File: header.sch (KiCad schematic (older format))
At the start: 19 parts, among them J1 Conn_01x10, J2 Conn_01x08, J3 Conn_01x06, J4 Conn_01x08, SW6 SW_Push, U1 ICE40HX4K-TQ144, U8 TXS0108EPW, U9 TXS0108EPW

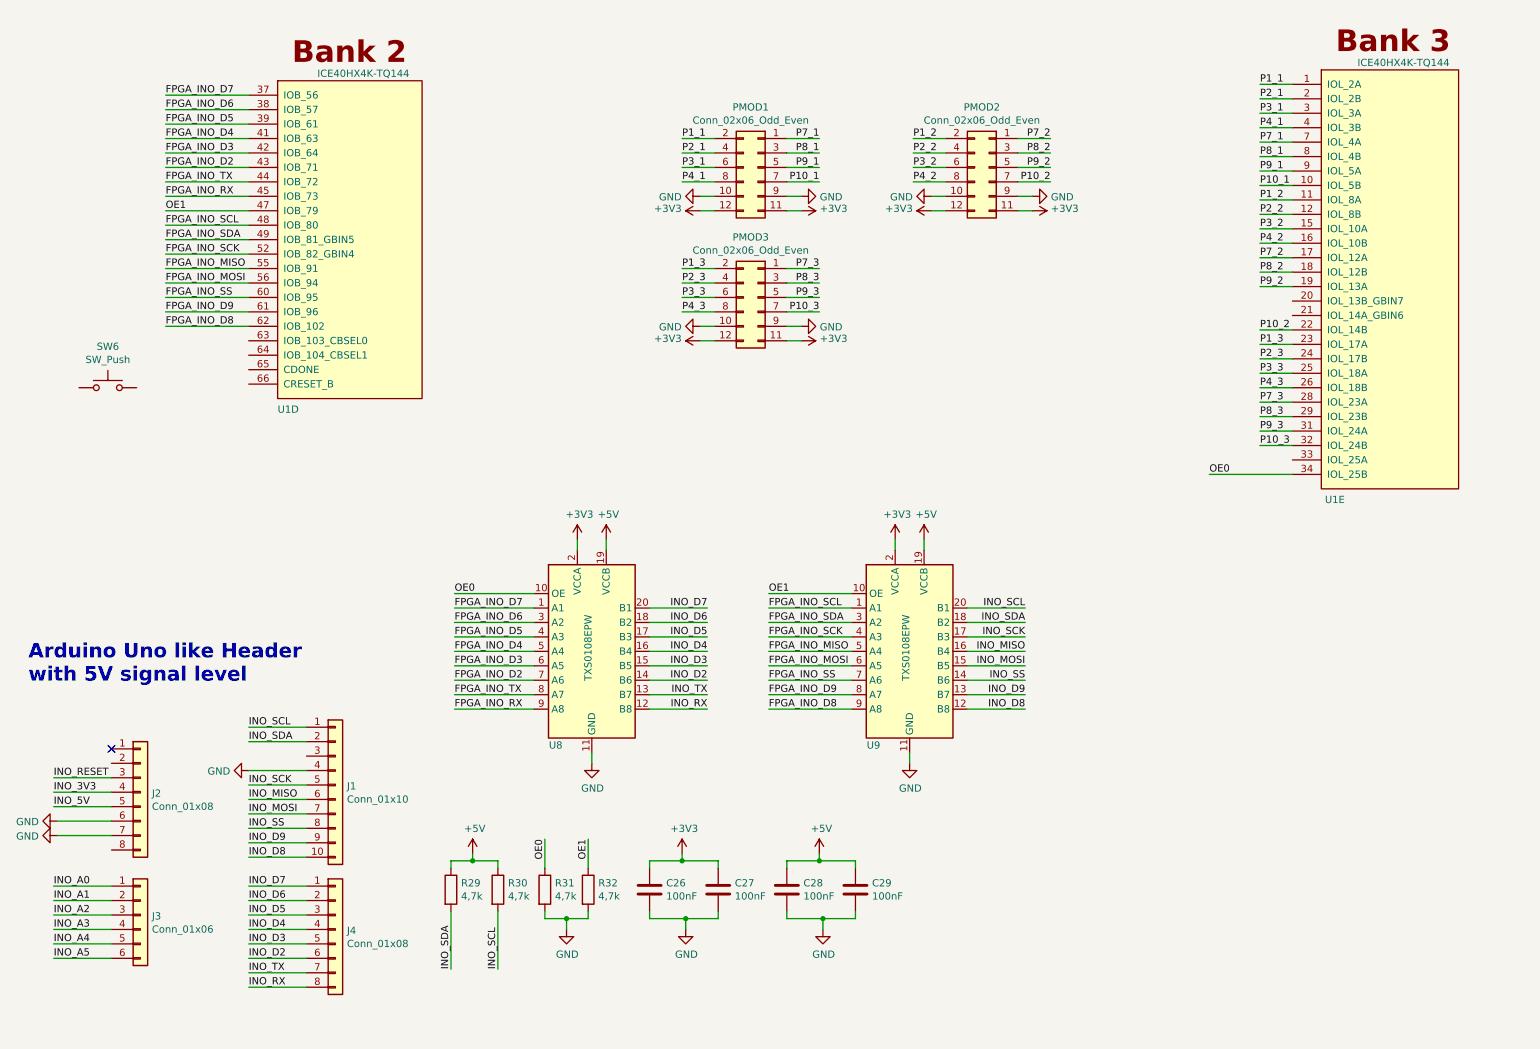
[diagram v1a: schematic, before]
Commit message: Continued on Programmer, moved the header signals around the package to free some space for a fully featured UART/RS232(TTL)
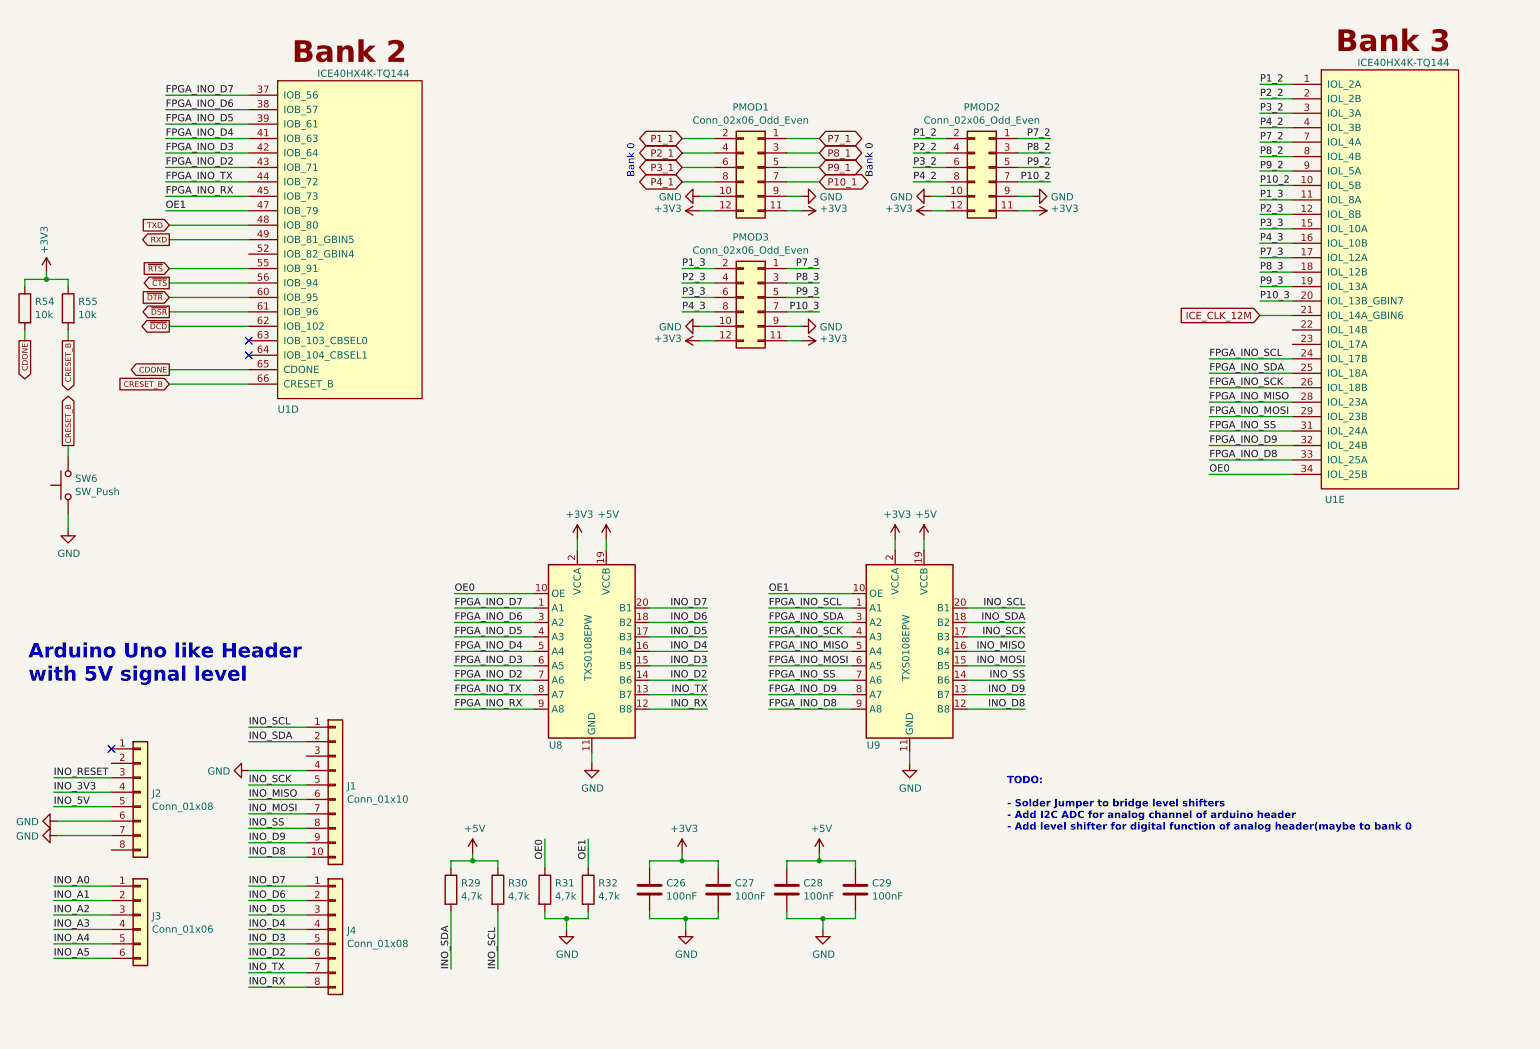
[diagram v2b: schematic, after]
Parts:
- added R54, R55: 10k, Resistor_SMD:R_0603_1608Metric, symbol Device:R
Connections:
- net +3V3: now also R54.1, R55.1
- net FPGA_INO_D8: now also U1.33 (IOL_25A); no longer U1.62 (IOB_102)
- net FPGA_INO_D9: now also U1.32 (IOL_24B); no longer U1.61 (IOB_96)
- net FPGA_INO_MISO: now also U1.28 (IOL_23A); no longer U1.55 (IOB_91)
- net FPGA_INO_MOSI: now also U1.29 (IOL_23B); no longer U1.56 (IOB_94)
- net FPGA_INO_SCK: now also U1.26 (IOL_18B); no longer U1.52 (IOB_82_GBIN4)
- net FPGA_INO_SCL: now also U1.24 (IOL_17B); no longer U1.48 (IOB_80)
- net FPGA_INO_SDA: now also U1.25 (IOL_18A); no longer U1.49 (IOB_81_GBIN5)
- net FPGA_INO_SS: now also U1.31 (IOL_24A); no longer U1.60 (IOB_95)
- net GND: now also SW6.1
- net P10_1: no longer U1.10 (IOL_5B)
- net P10_2: now also U1.10 (IOL_5B); no longer U1.22 (IOL_14B)
- net P10_3: now also U1.20 (IOL_13B_GBIN7); no longer U1.32 (IOL_24B)
- net P1_1: no longer U1.1 (IOL_2A)
- net P1_2: now also U1.1 (IOL_2A); no longer U1.11 (IOL_8A)
- net P1_3: now also U1.11 (IOL_8A); no longer U1.23 (IOL_17A)
- net P2_1: no longer U1.2 (IOL_2B)
- net P2_2: now also U1.2 (IOL_2B); no longer U1.12 (IOL_8B)
- net P2_3: now also U1.12 (IOL_8B); no longer U1.24 (IOL_17B)
- net P3_1: no longer U1.3 (IOL_3A)
- net P3_2: now also U1.3 (IOL_3A); no longer U1.15 (IOL_10A)
- net P3_3: now also U1.15 (IOL_10A); no longer U1.25 (IOL_18A)
- net P4_1: no longer U1.4 (IOL_3B)
- net P4_2: now also U1.4 (IOL_3B); no longer U1.16 (IOL_10B)
- net P4_3: now also U1.16 (IOL_10B); no longer U1.26 (IOL_18B)
- net P7_1: no longer U1.7 (IOL_4A)
- net P7_2: now also U1.7 (IOL_4A); no longer U1.17 (IOL_12A)
- net P7_3: now also U1.17 (IOL_12A); no longer U1.28 (IOL_23A)
- net P8_1: no longer U1.8 (IOL_4B)
- net P8_2: now also U1.8 (IOL_4B); no longer U1.18 (IOL_12B)
- net P8_3: now also U1.18 (IOL_12B); no longer U1.29 (IOL_23B)
- net P9_1: no longer U1.9 (IOL_5A)
- net P9_2: now also U1.9 (IOL_5A); no longer U1.19 (IOL_13A)
- net P9_3: now also U1.19 (IOL_13A); no longer U1.31 (IOL_24A)
- net ICE_CLK_12M: now reaches U1.21 (IOL_14A_GBIN6)
- net CDONE: now reaches U1.65 (CDONE)
- net CDONE: now also R54.2
- net CRESET_B: now reaches U1.66 (CRESET_B)
- net CRESET_B: now also SW6.2, R55.2
- new net RXD: U1.49 (IOB_81_GBIN5)
- new net TXD: U1.48 (IOB_80)
- new net ~CTS~: U1.56 (IOB_94)
- new net ~DCD~: U1.62 (IOB_102)
- new net ~DSR~: U1.61 (IOB_96)
- new net ~DTR~: U1.60 (IOB_95)
- new net ~RTS~: U1.55 (IOB_91)
- no-connect marks 1 -> 3
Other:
- note added: "Bank 0"
- note added: "TODO:\n\n- Solder Jumper to bridge level shifters\n- Add I2C ADC for analog channel of arduino header\n- Add level shifter for digital function of analog header(maybe to bank 0"
- moved on the sheet: SW6
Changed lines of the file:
@@
-$EndComp
-$Comp
-L Switch:SW_Push SW?
-U 1 1 5CB172CF
-P 1350 3125
-AR Path="/5CAB7CD4/5CB172CF" Ref="SW?"  Part="1"
-AR Path="/5CB5889B/5CB172CF" Ref="SW6"  Part="1"
-F 0 "SW6" H 1350 3410 50  0000 C CNN
-F 1 "SW_Push" H 1350 3319 50  0000 C CNN
-F 2 "footprints:SW_SPST_TL3305A" H 1350 3325 50  0001 C CNN
-F 3 "http://spec_sheets.e-switch.com/specs/P010468.pdf" H 1350 3325 50  0001 C CNN
-F 4 "E-Switch" H 1350 3125 50  0001 C CNN "Mfg Name"
-F 5 "TL3305AF160QG" H 1350 3125 50  0001 C CNN "Mfg Part Num"
-F 6 "EG5350CT-ND" H 1350 3125 50  0001 C CNN "Digikey"
-F 7 "SWITCH TACTILE SPST-NO 50MA 12V" H 1350 3125 50  0001 C CNN "Description"
-	1    1350 3125
-	1    0    0    -1
 $EndComp
 $Comp
@@
 Wire Wire Line
 	1750 1900 2325 1900
-Text Label 1750 2100 0    50   ~ 0
+Text Label 8975 3025 0    50   ~ 0
 FPGA_INO_SDA
 Wire Wire Line
-	1750 2100 2325 2100
-Text Label 1750 2000 0    50   ~ 0
+	8975 3025 9550 3025
+Text Label 8975 2925 0    50   ~ 0
 FPGA_INO_SCL
 Wire Wire Line
-	1750 2000 2325 2000
-Text Label 1750 2700 0    50   ~ 0
+	8975 2925 9550 2925
+Text Label 8975 3625 0    50   ~ 0
 FPGA_INO_D8
 Wire Wire Line
-	1750 2700 2325 2700
-Text Label 1750 2600 0    50   ~ 0
+	8975 3625 9550 3625
+Text Label 8975 3525 0    50   ~ 0
 FPGA_INO_D9
 Wire Wire Line
-	1750 2600 2325 2600
-Text Label 1750 2500 0    50   ~ 0
+	8975 3525 9550 3525
+Text Label 8975 3425 0    50   ~ 0
 FPGA_INO_SS
 Wire Wire Line
-	1750 2500 2325 2500
-Text Label 1750 2400 0    50   ~ 0
+	8975 3425 9550 3425
+Text Label 8975 3325 0    50   ~ 0
 FPGA_INO_MOSI
 Wire Wire Line
-	1750 2400 2325 2400
-Text Label 1750 2300 0    50   ~ 0
+	8975 3325 9550 3325
+Text Label 8975 3225 0    50   ~ 0
 FPGA_INO_MISO
 Wire Wire Line
-	1750 2300 2325 2300
-Text Label 1750 2200 0    50   ~ 0
+	8975 3225 9550 3225
+Text Label 8975 3125 0    50   ~ 0
 FPGA_INO_SCK
 Wire Wire Line
-	1750 2200 2325 2200
+	8975 3125 9550 3125
 Text Label 8975 3725 0    50   ~ 0
 OE0
@@
 $Comp
 L Device:C C?
-U 1 1 5CD4AF05
-P 5100 6600
-AR Path="/5CAB7CD4/5CD4AF05" Ref="C?"  Part="1"
-AR Path="/5CB5889B/5CD4AF05" Ref="C26"  Part="1"
-F 0 "C26" H 5215 6646 50  0000 L CNN
-F 1 "100nF" H 5215 6555 50  0000 L CNN
-F 2 "Capacitor_SMD:C_0603_1608Metric" H 5138 6450 50  0001 C CNN
-F 3 "~" H 5100 6600 50  0001 C CNN
-	1    5100 6600
-	1    0    0    -1
-$EndComp
-$Comp
-L Device:C C?
 U 1 1 5CD4ED57
 P 5575 6600
@@
 	-1   0    0    -1
 $EndComp
-Text Label 5325 1400 0    50   ~ 0
-P1_1
 Wire Wire Line
 	5325 1400 5550 1400
-Text Label 5325 1500 0    50   ~ 0
-P2_1
 Wire Wire Line
 	5325 1500 5550 1500
-Text Label 5325 1600 0    50   ~ 0
-P3_1
 Wire Wire Line
 	5325 1600 5550 1600
-Text Label 5325 1700 0    50   ~ 0
-P4_1
 Wire Wire Line
 	5325 1700 5550 1700
-Text Label 6275 1400 2    50   ~ 0
-P7_1
 Wire Wire Line
 	6275 1400 6050 1400
-Text Label 6275 1500 2    50   ~ 0
-P8_1
 Wire Wire Line
 	6275 1500 6050 1500
-Text Label 6275 1600 2    50   ~ 0
-P9_1
 Wire Wire Line
 	6275 1600 6050 1600
-Text Label 6275 1700 2    50   ~ 0
-P10_1
 Wire Wire Line
 	6275 1700 6050 1700
@@
 	-1   0    0    -1
 $EndComp
-Text Label 6925 1400 0    50   ~ 0
-P1_2
 Wire Wire Line
 	6925 1400 7150 1400
@@
 	6275 2600 6050 2600
 Text Label 9325 1025 0    50   ~ 0
-P1_1
+P1_2
 Wire Wire Line
 	9325 1025 9550 1025
 Text Label 9325 1125 0    50   ~ 0
-P2_1
+P2_2
 Wire Wire Line
 	9325 1125 9550 1125
 Text Label 9325 1225 0    50   ~ 0
-P3_1
+P3_2
 Wire Wire Line
 	9325 1225 9550 1225
 Text Label 9325 1325 0    50   ~ 0
-P4_1
+P4_2
 Wire Wire Line
 	9325 1325 9550 1325
 Text Label 9325 1425 0    50   ~ 0
-P7_1
+P7_2
 Wire Wire Line
 	9325 1425 9550 1425
 Text Label 9325 1525 0    50   ~ 0
-P8_1
+P8_2
 Wire Wire Line
 	9325 1525 9550 1525
 Text Label 9325 1625 0    50   ~ 0
-P9_1
+P9_2
 Wire Wire Line
 	9325 1625 9550 1625
 Text Label 9325 1725 0    50   ~ 0
-P10_1
+P10_2
 Wire Wire Line
 	9325 1725 9550 1725
 Text Label 9325 1825 0    50   ~ 0
-P1_2
+P1_3
 Wire Wire Line
 	9325 1825 9550 1825
 Text Label 9325 1925 0    50   ~ 0
-P2_2
+P2_3
 Wire Wire Line
 	9325 1925 9550 1925
 Text Label 9325 2025 0    50   ~ 0
-P3_2
+P3_3
 Wire Wire Line
 	9325 2025 9550 2025
 Text Label 9325 2125 0    50   ~ 0
-P4_2
+P4_3
 Wire Wire Line
 	9325 2125 9550 2125
 Text Label 9325 2225 0    50   ~ 0
-P7_2
+P7_3
 Wire Wire Line
 	9325 2225 9550 2225
 Text Label 9325 2325 0    50   ~ 0
-P8_2
+P8_3
 Wire Wire Line
 	9325 2325 9550 2325
 Text Label 9325 2425 0    50   ~ 0
-P9_2
+P9_3
 Wire Wire Line
 	9325 2425 9550 2425
-Text Label 9325 2725 0    50   ~ 0
-P10_2
-Wire Wire Line
-	9325 2725 9550 2725
-Text Label 9325 2825 0    50   ~ 0
-P1_3
-Wire Wire Line
-	9325 2825 9550 2825
-Text Label 9325 2925 0    50   ~ 0
-P2_3
-Wire Wire Line
-	9325 2925 9550 2925
-Text Label 9325 3025 0    50   ~ 0
-P3_3
-Wire Wire Line
-	9325 3025 9550 3025
-Text Label 9325 3125 0    50   ~ 0
-P4_3
-Wire Wire Line
-	9325 3125 9550 3125
-Text Label 9325 3225 0    50   ~ 0
-P7_3
-Wire Wire Line
-	9325 3225 9550 3225
-Text Label 9325 3325 0    50   ~ 0
-P8_3
-Wire Wire Line
-	9325 3325 9550 3325
-Text Label 9325 3425 0    50   ~ 0
-P9_3
-Wire Wire Line
-	9325 3425 9550 3425
-Text Label 9325 3525 0    50   ~ 0
+Text Label 9325 2525 0    50   ~ 0
 P10_3
 Wire Wire Line
-	9325 3525 9550 3525
+	9325 2525 9550 2525
+Text Notes 7575 6200 0    50   ~ 10
+TODO:\n\n- Solder Jumper to bridge level shifters\n- Add I2C ADC for analog channel of arduino header\n- Add level shifter for digital function of analog header(maybe to bank 0
+Text GLabel 1775 2000 0    39   Input ~ 0
+TXD
+Text GLabel 1775 2100 0    39   Output ~ 0
+RXD
+Text GLabel 1775 2300 0    39   Input ~ 0
+~RTS~
+Text GLabel 1775 2400 0    39   Output ~ 0
+~CTS~
+Text GLabel 1775 2500 0    39   Input ~ 0
+~DTR~
+Text GLabel 1775 2600 0    39   Output ~ 0
+~DSR~
+Text GLabel 1775 2700 0    39   Output ~ 0
+~DCD~
+Text Label 6925 1400 0    50   ~ 0
+P1_2
+Text GLabel 5325 1400 0    50   BiDi ~ 0
+P1_1
+Text GLabel 5325 1500 0    50   BiDi ~ 0
+P2_1
+Text GLabel 5325 1600 0    50   BiDi ~ 0
+P3_1
+Text GLabel 5325 1700 0    50   BiDi ~ 0
+P4_1
+Text GLabel 6275 1400 2    50   BiDi ~ 0
+P7_1
+Text GLabel 6275 1500 2    50   BiDi ~ 0
+P8_1
+Text GLabel 6275 1600 2    50   BiDi ~ 0
+P9_1
+Text GLabel 6275 1700 2    50   BiDi ~ 0
+P10_1
+Wire Wire Line
+	2325 2700 1775 2700
+Wire Wire Line
+	1775 2600 2325 2600
+Wire Wire Line
+	2325 2500 1775 2500
+Wire Wire Line
+	1775 2400 2325 2400
+Wire Wire Line
+	2325 2300 1775 2300
+Wire Wire Line
+	1775 2000 2325 2000
+Wire Wire Line
+	2325 2100 1775 2100
+Text Notes 5000 1675 1    50   ~ 0
+Bank 0
+Text Notes 6650 1675 1    50   ~ 0
+Bank 0
+Connection ~ 925  2375
+Wire Wire Line
+	925  2325 925  2375
+$Comp
+L power:+3V3 #PWR?
+U 1 1 5D05805B
+P 925 2325
+AR Path="/5CAB8B22/5D05805B" Ref="#PWR?"  Part="1"
+AR Path="/5CB5889B/5D05805B" Ref="#PWR0135"  Part="1"
+F 0 "#PWR0135" H 925 2175 50  0001 C CNN
+F 1 "+3V3" V 940 2453 50  0000 L CNN
+F 2 "" H 925 2325 50  0001 C CNN
+F 3 "" H 925 2325 50  0001 C CNN
+	1    925  2325
+	-1   0    0    -1
+$EndComp
+Wire Wire Line
+	775  2375 925  2375
+Wire Wire Line
+	775  2425 775  2375
+$Comp
+L Device:R R?
+U 1 1 5D058055
+P 775 2575
+AR Path="/5CAB8B22/5D058055" Ref="R?"  Part="1"
+AR Path="/5CB5889B/5D058055" Ref="R54"  Part="1"
+F 0 "R54" H 705 2621 50  0000 R CNN
+F 1 "10k" H 705 2530 50  0000 R CNN
+F 2 "Resistor_SMD:R_0603_1608Metric" V 705 2575 50  0001 C CNN
+F 3 "~" H 775 2575 50  0001 C CNN
+	1    775  2575
+	-1   0    0    -1
+$EndComp
+Wire Wire Line
+	925  2375 1075 2375
+Wire Wire Line
+	1075 2375 1075 2425
+$Comp
+L Device:R R?
+U 1 1 5D058061
+P 1075 2575
+AR Path="/5CAB8B22/5D058061" Ref="R?"  Part="1"
+AR Path="/5CB5889B/5D058061" Ref="R55"  Part="1"
+F 0 "R55" H 1005 2621 50  0000 R CNN
+F 1 "10k" H 1005 2530 50  0000 R CNN
+F 2 "Resistor_SMD:R_0603_1608Metric" V 1005 2575 50  0001 C CNN
+F 3 "~" H 1075 2575 50  0001 C CNN
+	1    1075 2575
+	-1   0    0    -1
+$EndComp
+Wire Wire Line
+	1775 3000 2325 3000
+Wire Wire Line
+	2325 3100 1775 3100
+Text GLabel 1775 3100 0    39   Input ~ 0
+CRESET_B
+Text GLabel 1775 3000 0    39   Output ~ 0
+CDONE
+Text GLabel 1075 2800 3    39   Output ~ 0
+CRESET_B
+Text GLabel 775  2800 3    39   Output ~ 0
+CDONE
+Wire Wire Line
+	1075 2800 1075 2725
+Wire Wire Line
+	775  2800 775  2725
+Wire Wire Line
+	1075 4100 1075 4000
+$Comp
+L power:GND #PWR0136
+U 1 1 5D1576AB
+P 1075 4100
+F 0 "#PWR0136" H 1075 3850 50  0001 C CNN
+F 1 "GND" H 1080 3927 50  0000 C CNN
+F 2 "" H 1075 4100 50  0001 C CNN
+F 3 "" H 1075 4100 50  0001 C CNN
+	1    1075 4100
+	1    0    0    -1
+$EndComp
+Wire Wire Line
+	1075 3525 1075 3600
+Text GLabel 1075 3525 1    39   Output ~ 0
+CRESET_B
+$Comp
+L Switch:SW_Push SW?
+U 1 1 5CB172CF
+P 1075 3800
+AR Path="/5CAB7CD4/5CB172CF" Ref="SW?"  Part="1"
+AR Path="/5CB5889B/5CB172CF" Ref="SW6"  Part="1"
+F 0 "SW6" V 1121 3752 50  0000 R CNN
+F 1 "SW_Push" V 1030 3752 50  0000 R CNN
+F 2 "footprints:SW_SPST_TL3305A" H 1075 4000 50  0001 C CNN
+F 3 "http://spec_sheets.e-switch.com/specs/P010468.pdf" H 1075 4000 50  0001 C CNN
+F 4 "E-Switch" H 1075 3800 50  0001 C CNN "Mfg Name"
+F 5 "TL3305AF160QG" H 1075 3800 50  0001 C CNN "Mfg Part Num"
+F 6 "EG5350CT-ND" H 1075 3800 50  0001 C CNN "Digikey"
+F 7 "SWITCH TACTILE SPST-NO 50MA 12V" H 1075 3800 50  0001 C CNN "Description"
+	1    1075 3800
+	0    -1   -1   0
+$EndComp
+NoConn ~ 2325 2800
+NoConn ~ 2325 2900
+Text GLabel 9325 2625 0    50   Input ~ 0
+ICE_CLK_12M
+Wire Wire Line
+	9325 2625 9550 2625
+$Comp
+L Device:C C?
+U 1 1 5CD4AF05
+P 5100 6600
+AR Path="/5CAB7CD4/5CD4AF05" Ref="C?"  Part="1"
+AR Path="/5CB5889B/5CD4AF05" Ref="C26"  Part="1"
+F 0 "C26" H 5215 6646 50  0000 L CNN
+F 1 "100nF" H 5215 6555 50  0000 L CNN
+F 2 "Capacitor_SMD:C_0603_1608Metric" H 5138 6450 50  0001 C CNN
+F 3 "~" H 5100 6600 50  0001 C CNN
+	1    5100 6600
+	1    0    0    -1
+$EndComp
 $EndSCHEMATC
